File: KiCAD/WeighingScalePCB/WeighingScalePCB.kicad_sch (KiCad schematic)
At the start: 75 parts, among them IC1 MAX6675ISA+T, IC2 APS11753KMDALX-9PL5, J1 Conn_01x14_MountingPin, J2 AudioJack4, J4 Battery Conn, J6 Conn_01x04_MountingPin, Q2 NX138AKR, Q3 NX138AKR, Q4 NX138AKR, Q5 NX138AKR, T1 TouchPad, T2 TouchPad, U1 XIAO-ESP32-S3-SMD, U10 LMC555xMM, U2 HX711, U3 LMC555xMM, U4 74LVC1G79GW-Q100H, U5 TTP223-BA6, U6 TTP223-BA6, U7 74LVC1G79GW-Q100H, U8 74LVC1G04, U9 74LVC1G08

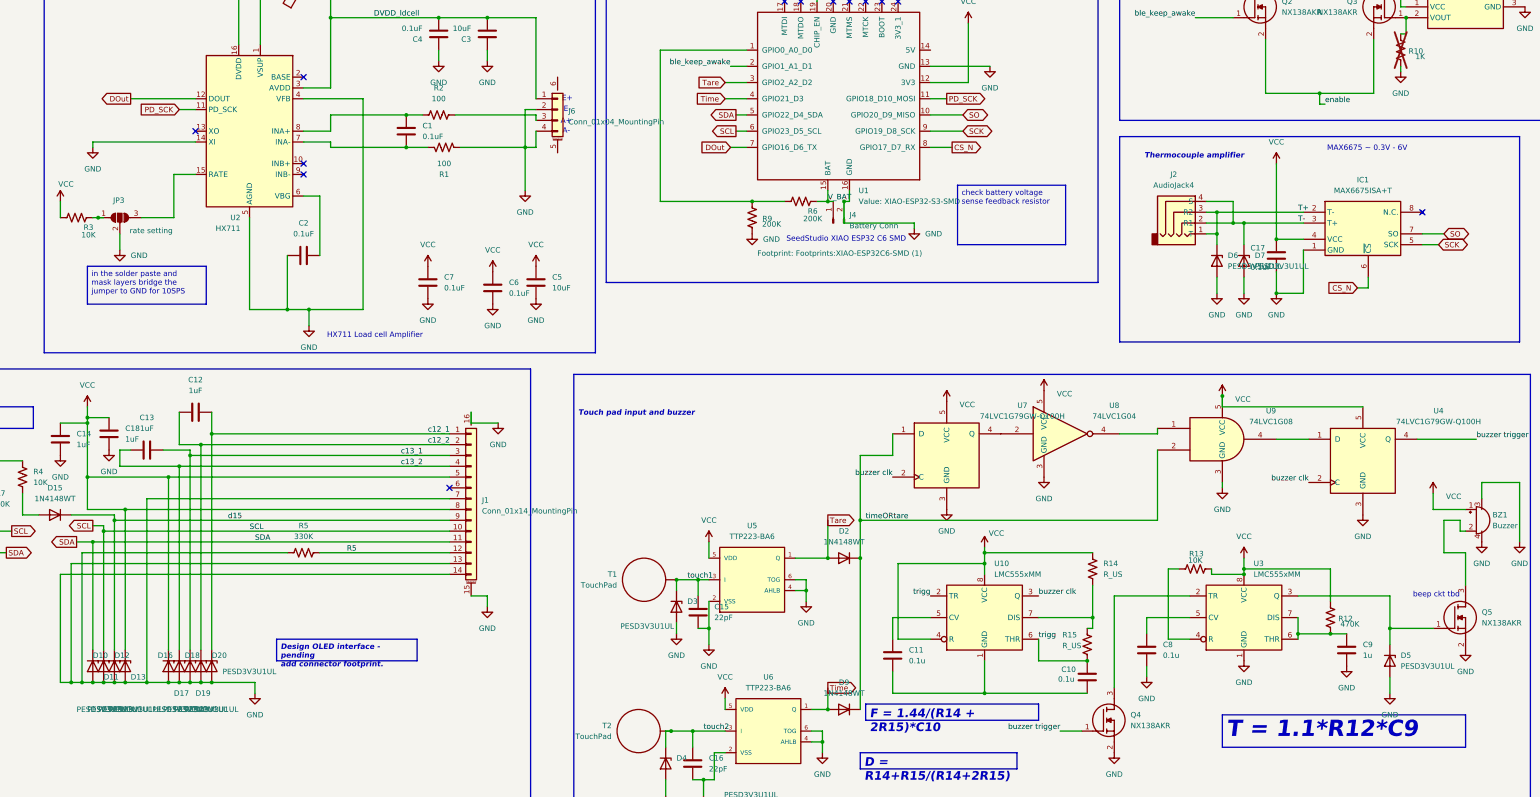
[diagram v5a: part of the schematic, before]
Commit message: layout done, decap placement and ferrite bead choice pending
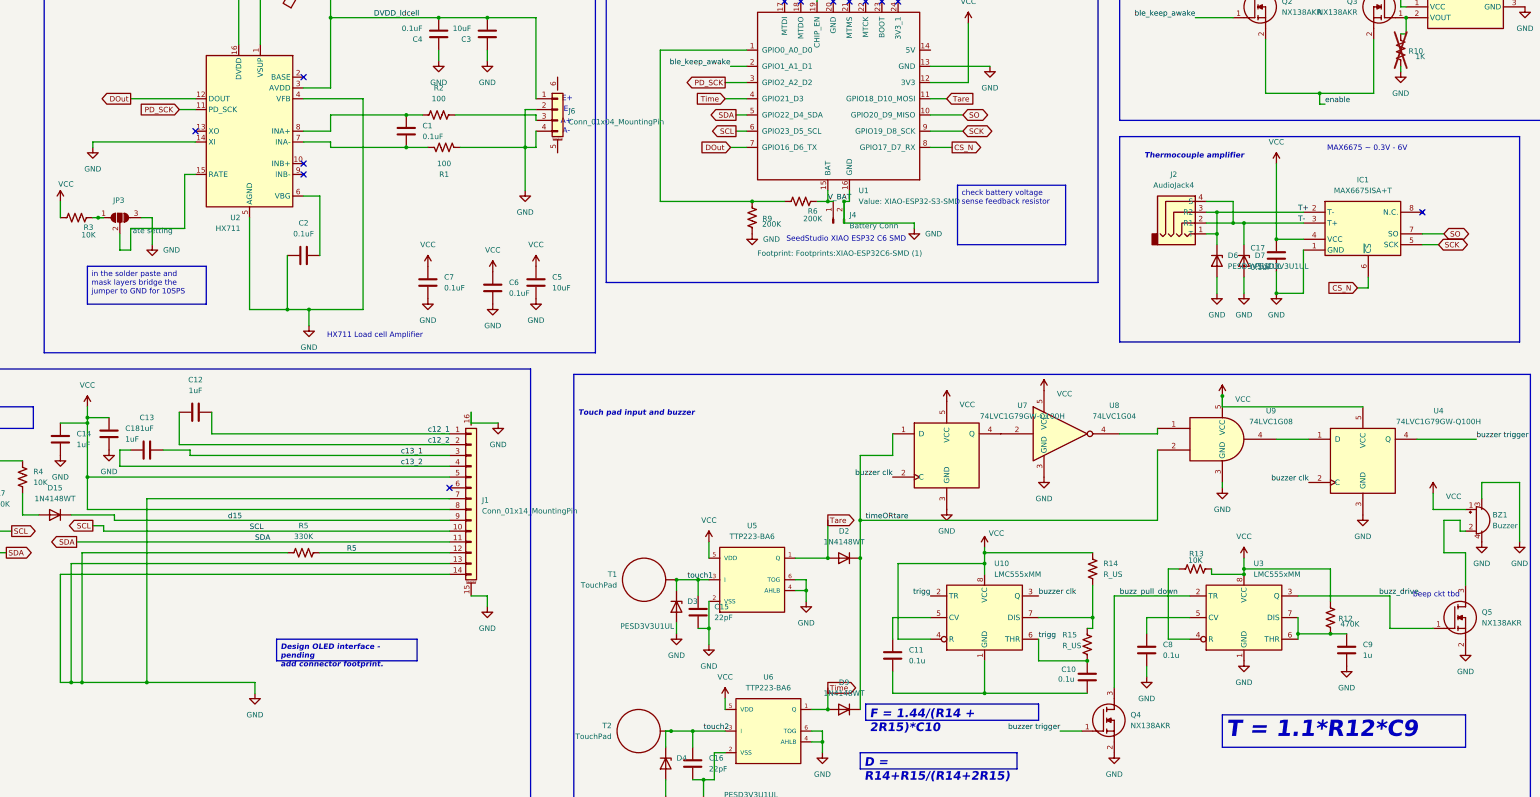
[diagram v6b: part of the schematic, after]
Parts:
- removed D10, D11, D12, D13, D16, D17, D18, D19, D20, D5: PESD3V3U1UL, Diode_SMD:D_SOD-882, symbol Diode:PESD3V3U1UL
- R7, R8: footprint Resistor_SMD:R_0402_1005Metric -> Resistor_SMD:R_0603_1608Metric
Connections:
- net GND: now also JP3.3 (B); no longer JP3.2 (C)
- net PD_SCK: now also U1.3 (GPIO2_A2_D2); no longer U1.11 (GPIO18_D10_MOSI)
- net Tare: now also U1.11 (GPIO18_D10_MOSI); no longer U1.3 (GPIO2_A2_D2)
- net buzz_drive: now reaches Q5.1 (G), U3.3 (Q)
- net buzz_pull_down: now reaches Q4.3 (D), U3.2 (TR)
- net at U2.15 (RATE): now also JP3.2 (C); no longer JP3.3 (B)

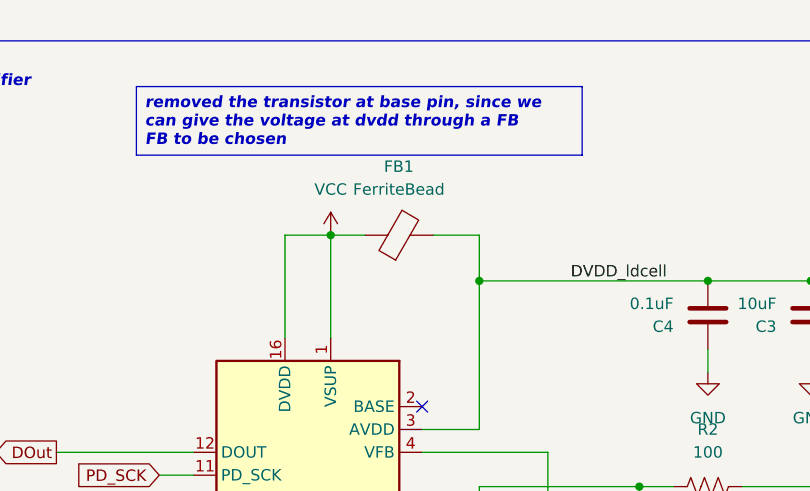
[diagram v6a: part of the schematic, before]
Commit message: fb removed, decaps will be sufficient, add more decaps, add cap between vbat and vcc
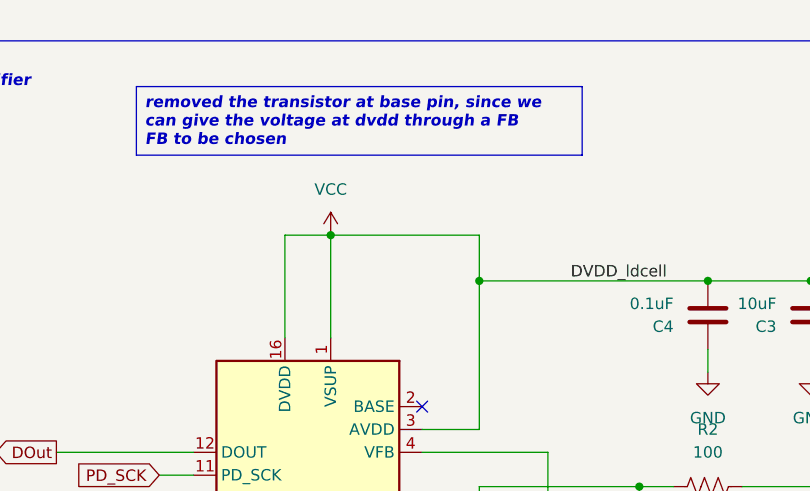
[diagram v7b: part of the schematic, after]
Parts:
- removed FB1: FerriteBead, symbol Device:FerriteBead
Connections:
- net DVDD_ldcell is gone; now on net VCC: C3.2, C4.2, J6.1 (Pin_1), U2.3 (AVDD)
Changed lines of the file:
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@@
 	(wire
 		(pts
-			(xy 102.87 39.37) (xy 106.68 39.37)
+			(xy 102.87 39.37) (xy 119.38 39.37)
 		)
 		(stroke
@@
 	(wire
 		(pts
-			(xy 114.3 39.37) (xy 119.38 39.37)
-		)
-		(stroke
-			(width 0)
-			(type default)
-		)
-	)
-	(wire
-		(pts
 			(xy 38.1 165.1) (xy 44.45 165.1)
 		)
@@
 					(unit 1)
 				)
-			)
-		)
-	)
-	(symbol
-		(lib_id "Device:FerriteBead")
-		(at 110.49 39.37 90)
-		(unit 1)
-		(exclude_from_sim no)
-		(in_bom yes)
-		(on_board yes)
-		(dnp no)
-		(fields_autoplaced yes)
-		(property "Reference" "FB1"
-			(at 110.4392 31.75 90)
-			(effects
-				(font
-					(size 1.27 1.27)
-				)
-			)
-		)
-		(property "Value" "FerriteBead"
-			(at 110.4392 34.29 90)
-			(effects
-				(font
-					(size 1.27 1.27)
-				)
-			)
-		)
-		(property "Footprint" ""
-			(at 110.49 41.148 90)
-			(effects
-				(font
-					(size 1.27 1.27)
-				)
-				(hide yes)
-			)
-		)
-		(property "Datasheet" "~"
-			(at 110.49 39.37 0)
-			(effects
-				(font
-					(size 1.27 1.27)
-				)
-				(hide yes)
-			)
-		)
-		(property "Description" "Ferrite bead"
-			(at 110.49 39.37 0)
-			(effects
-				(font
-					(size 1.27 1.27)
-				)
-				(hide yes)
-			)
-		)
-		(pin "2"
-		)
-		(pin "1"
-		)
-		(instances
-			(project ""
-				(path "/fb3b7c1c-1dc1-4229-b305-25c6e0b4dbdc"
-					(reference "FB1")
-					(unit 1)
-				)

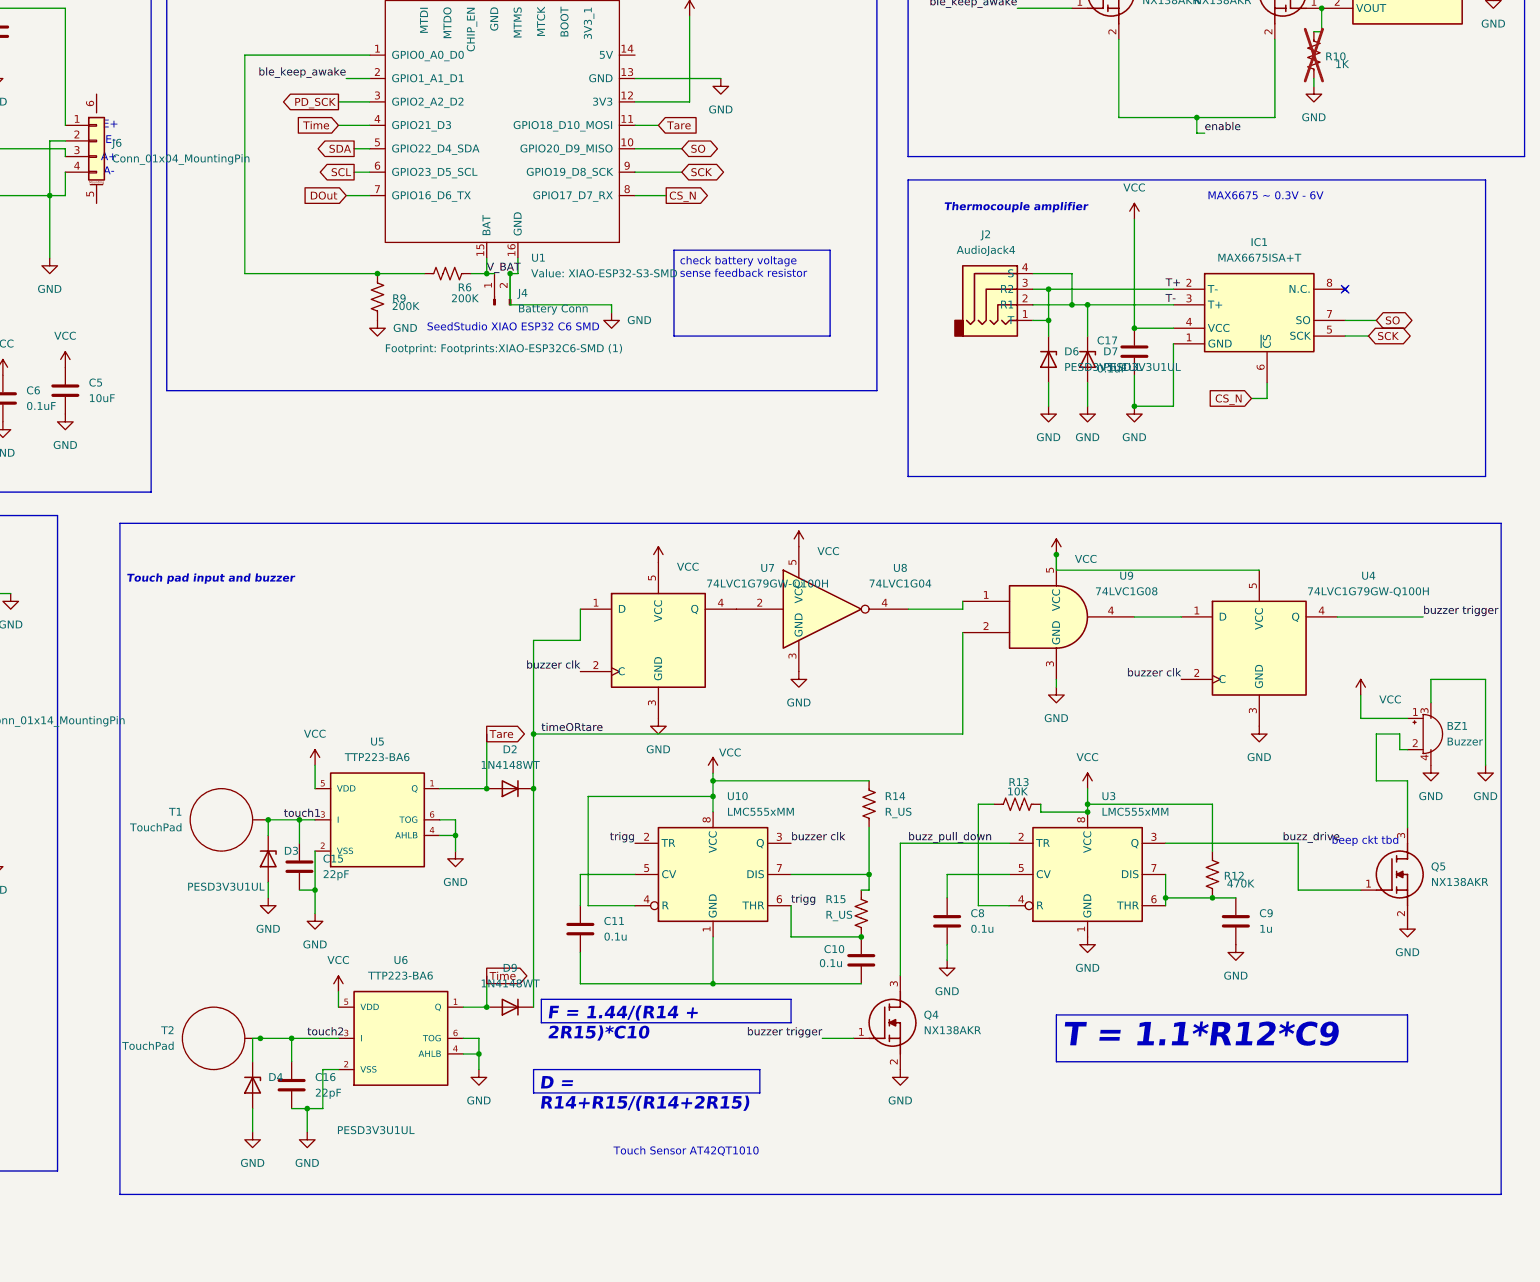
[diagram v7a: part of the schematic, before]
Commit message: changed touch sensor to CAP1203, yet to update in layout schematic done.
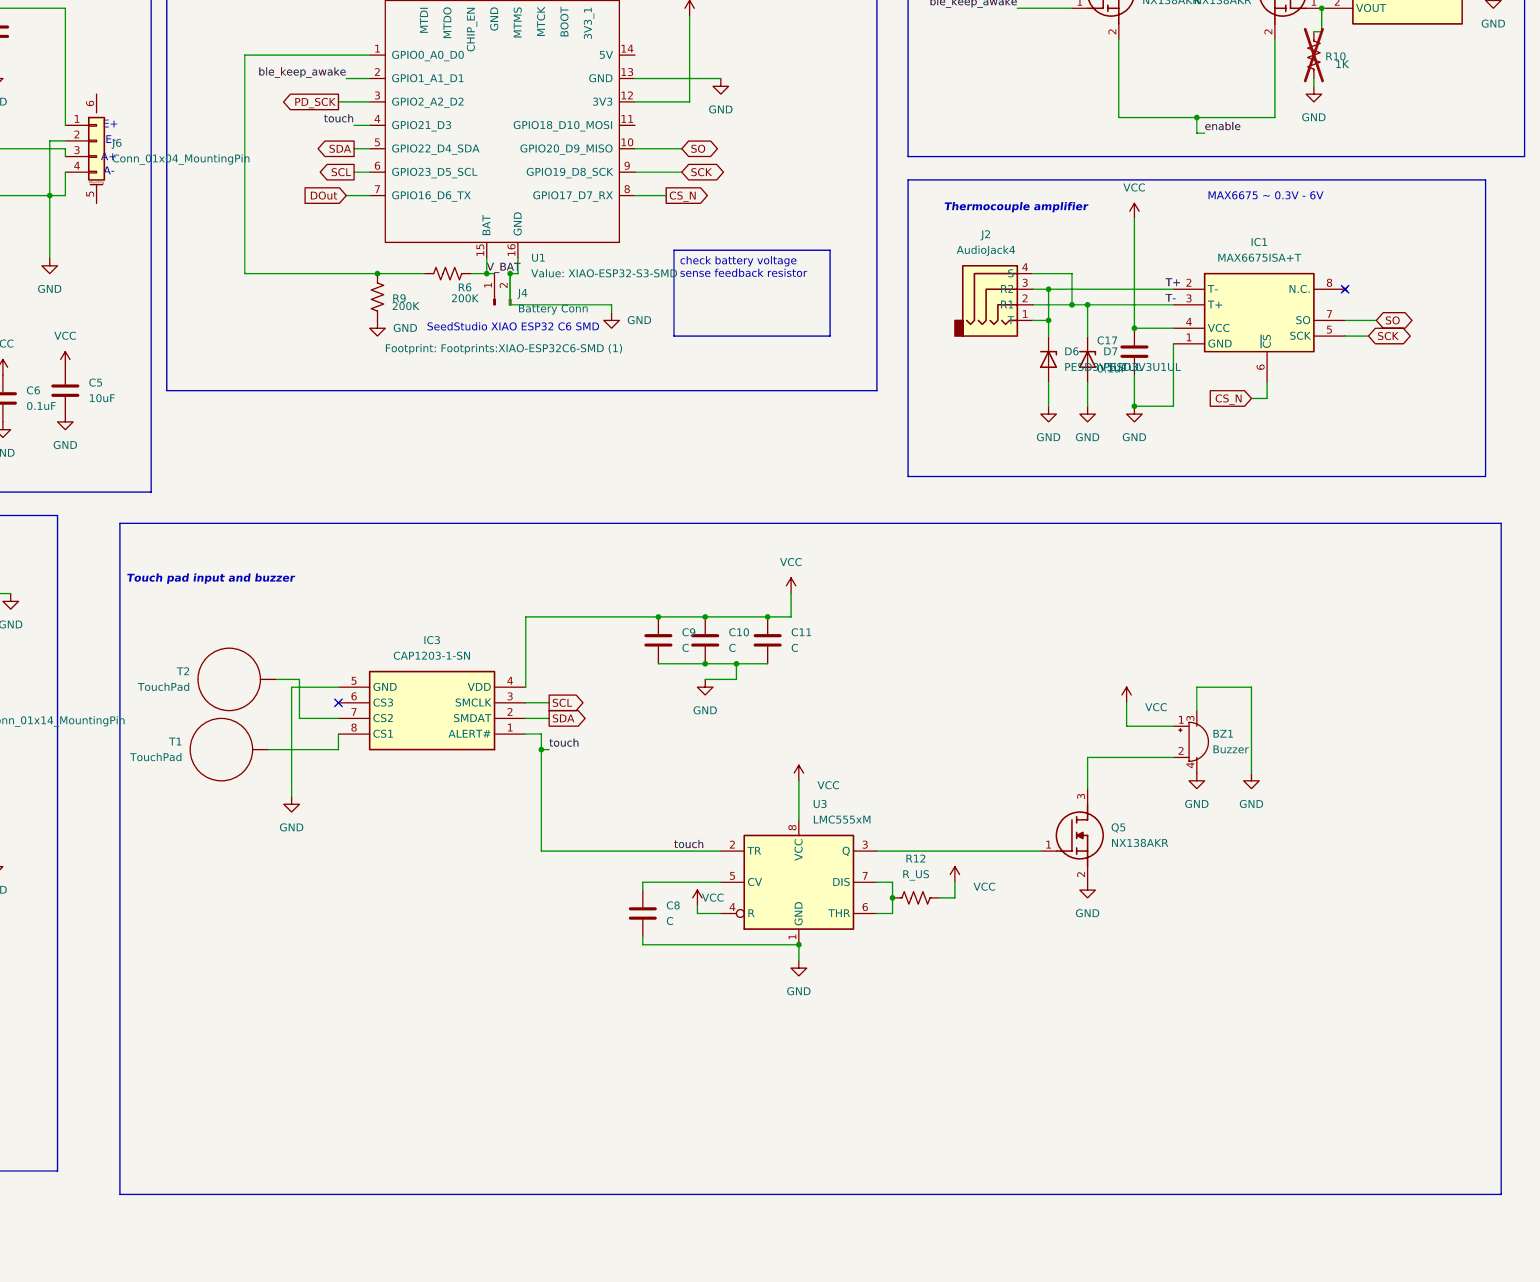
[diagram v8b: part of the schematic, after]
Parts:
- removed C15, C16: 22pF, Capacitor_SMD:C_0603_1608Metric, symbol Device:C
- removed D2, D9: 1N4148WT, Diode_SMD:D_SOD-523, symbol Diode:1N4148WT
- removed D3, D4: PESD3V3U1UL, Diode_SMD:D_SOD-882, symbol Diode:PESD3V3U1UL
- removed Q4: NX138AKR, Footprints:SOT95P230X110-3N, symbol NX138AKR Mosfet:NX138AKR
- removed R13: 10K, Resistor_SMD:R_0603_1608Metric, symbol Device:R_US
- removed R14, R15: R_US, Resistor_SMD:R_0603_1608Metric, symbol Device:R_US
- removed U10, U3: LMC555xMM, Package_SO:VSSOP-8_3x3mm_P0.65mm, symbol Timer:LMC555xMM
- removed U4, U7: 74LVC1G79GW-Q100H, Footprints:SOT65P212X110-5N_D_FF, symbol 74xGxx:74LVC1G79
- removed U5, U6: TTP223-BA6, Footprints:SOT23-6_touchpad_sensor, symbol TTP223-BA6:TTP223-BA6
- removed U8: 74LVC1G04, Footprints:SOT65P210X110-5N_NOT, symbol 74xGxx:74LVC1G04
- removed U9: 74LVC1G08, Footprints:SOT65P212X110-5N_AND, symbol 74xGxx:74LVC1G08
- added IC3: CAP1203-1-SN, SOIC127P600X175-8N, symbol CAP1203-1-SN:CAP1203-1-SN
- added U3: LMC555xM, Package_SO:SOIC-8_3.9x4.9mm_P1.27mm, symbol Timer:LMC555xM
- C10, C11, C8: value 0.1u -> C; footprint Capacitor_SMD:C_0603_1608Metric -> (none)
- C9: value 1u -> C; footprint Capacitor_SMD:C_0603_1608Metric -> (none)
- R12: value 470K -> R_US; footprint Resistor_SMD:R_0603_1608Metric -> (none)
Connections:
- net trigg is gone; now on net VCC: C10.1
- net GND: now also C10.2, C11.2, IC3.5 (GND), U3.1 (GND)
- net SCL: now also IC3.3 (SMCLK)
- net SDA: now also IC3.2 (SMDAT)
- net VCC: now also C11.1, C9.1, R12.2, IC3.4 (VDD), U3.4 (R), U3.8 (VCC); no longer R12.1
- net at C8.1: now also U3.5 (CV)
- net Tare: no longer names the net of U1.11 (GPIO18_D10_MOSI)
- net Time renamed touch
- net touch: now also IC3.1 (ALERT#), U3.2 (TR)
- net buzz_drive: no longer names the net of Q5.1 (G)
- net buzz_drive: now also U3.3 (Q)
- net touch1: no longer names the net of T1.T1 (Pad)
- net touch1: now also IC3.8 (CS1)
- net touch2: no longer names the net of T2.T2 (Pad)
- net touch2: now also IC3.7 (CS2)
- new net: R12.1, U3.6 (THR), U3.7 (DIS)
- no-connect marks 13 -> 14
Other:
- note removed: "Touch Sensor AT42QT1010"
- note removed: "beep ckt tbd"
- moved on the sheet: BZ1, Q5, T1, T2
